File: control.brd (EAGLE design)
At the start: 156 x 38 mm, 67 parts, among them IC3 ATTINY85-20S

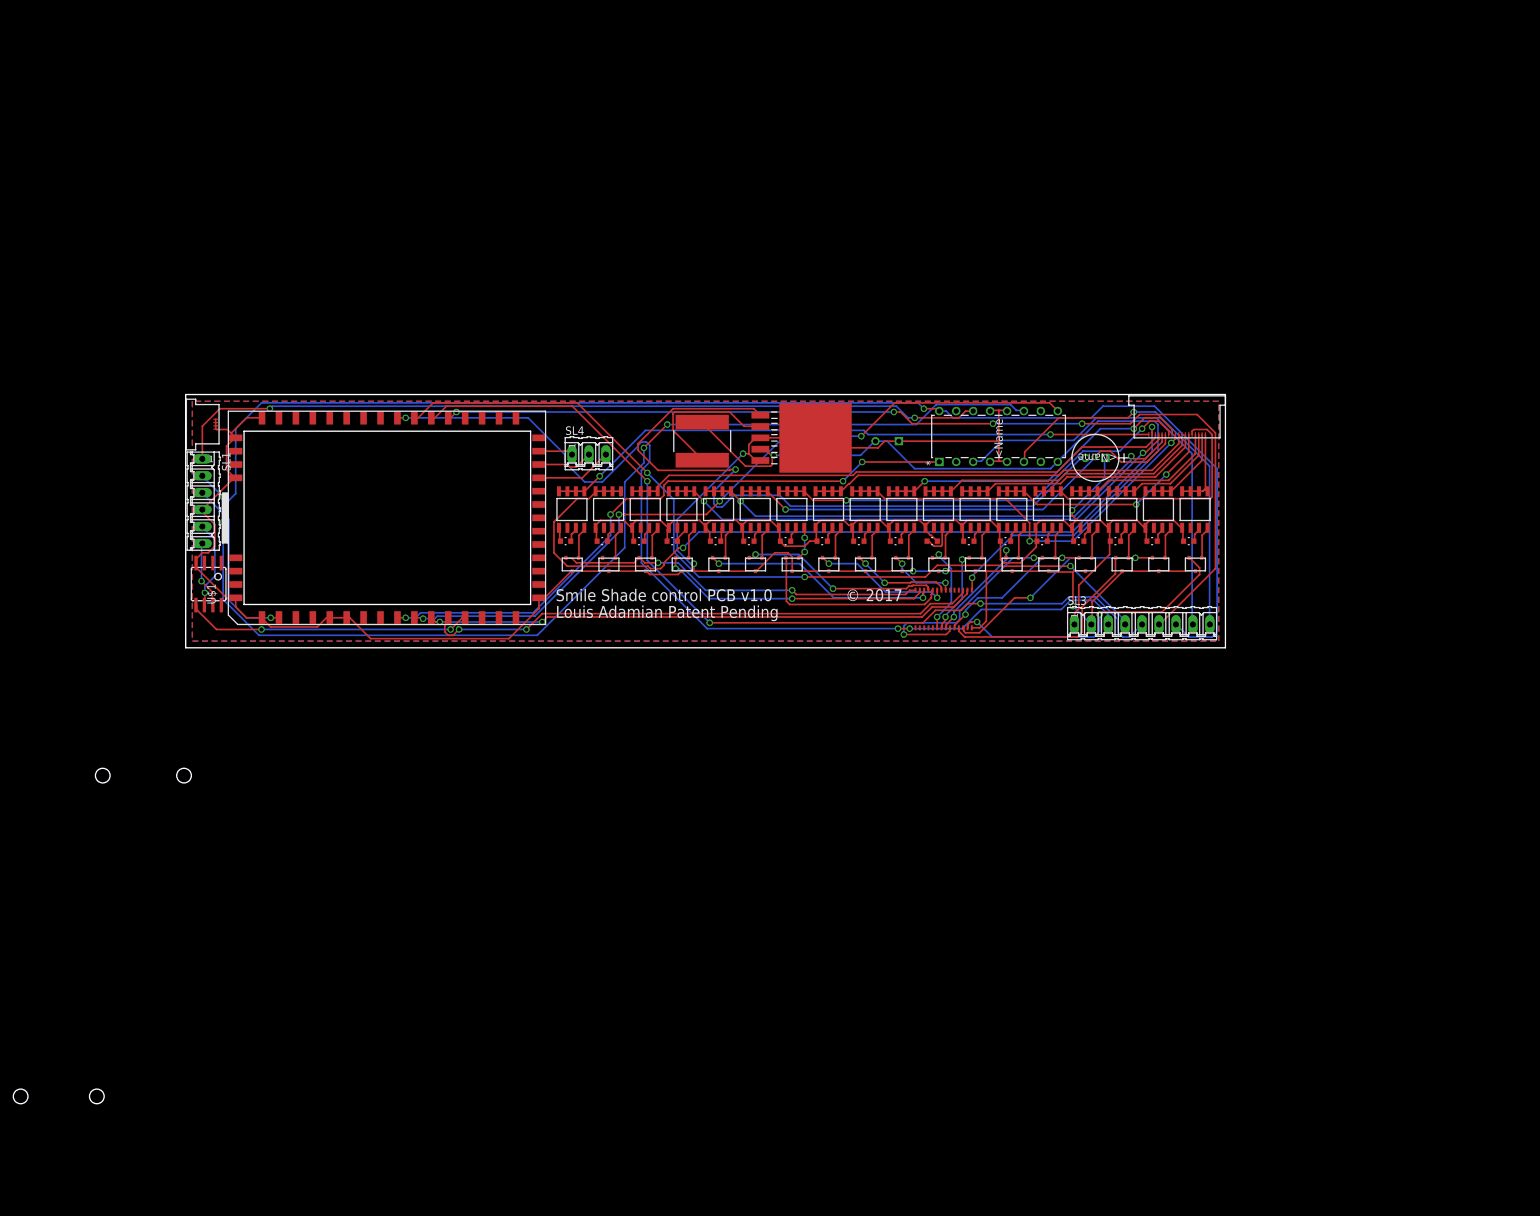
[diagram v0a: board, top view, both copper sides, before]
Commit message: adds new components
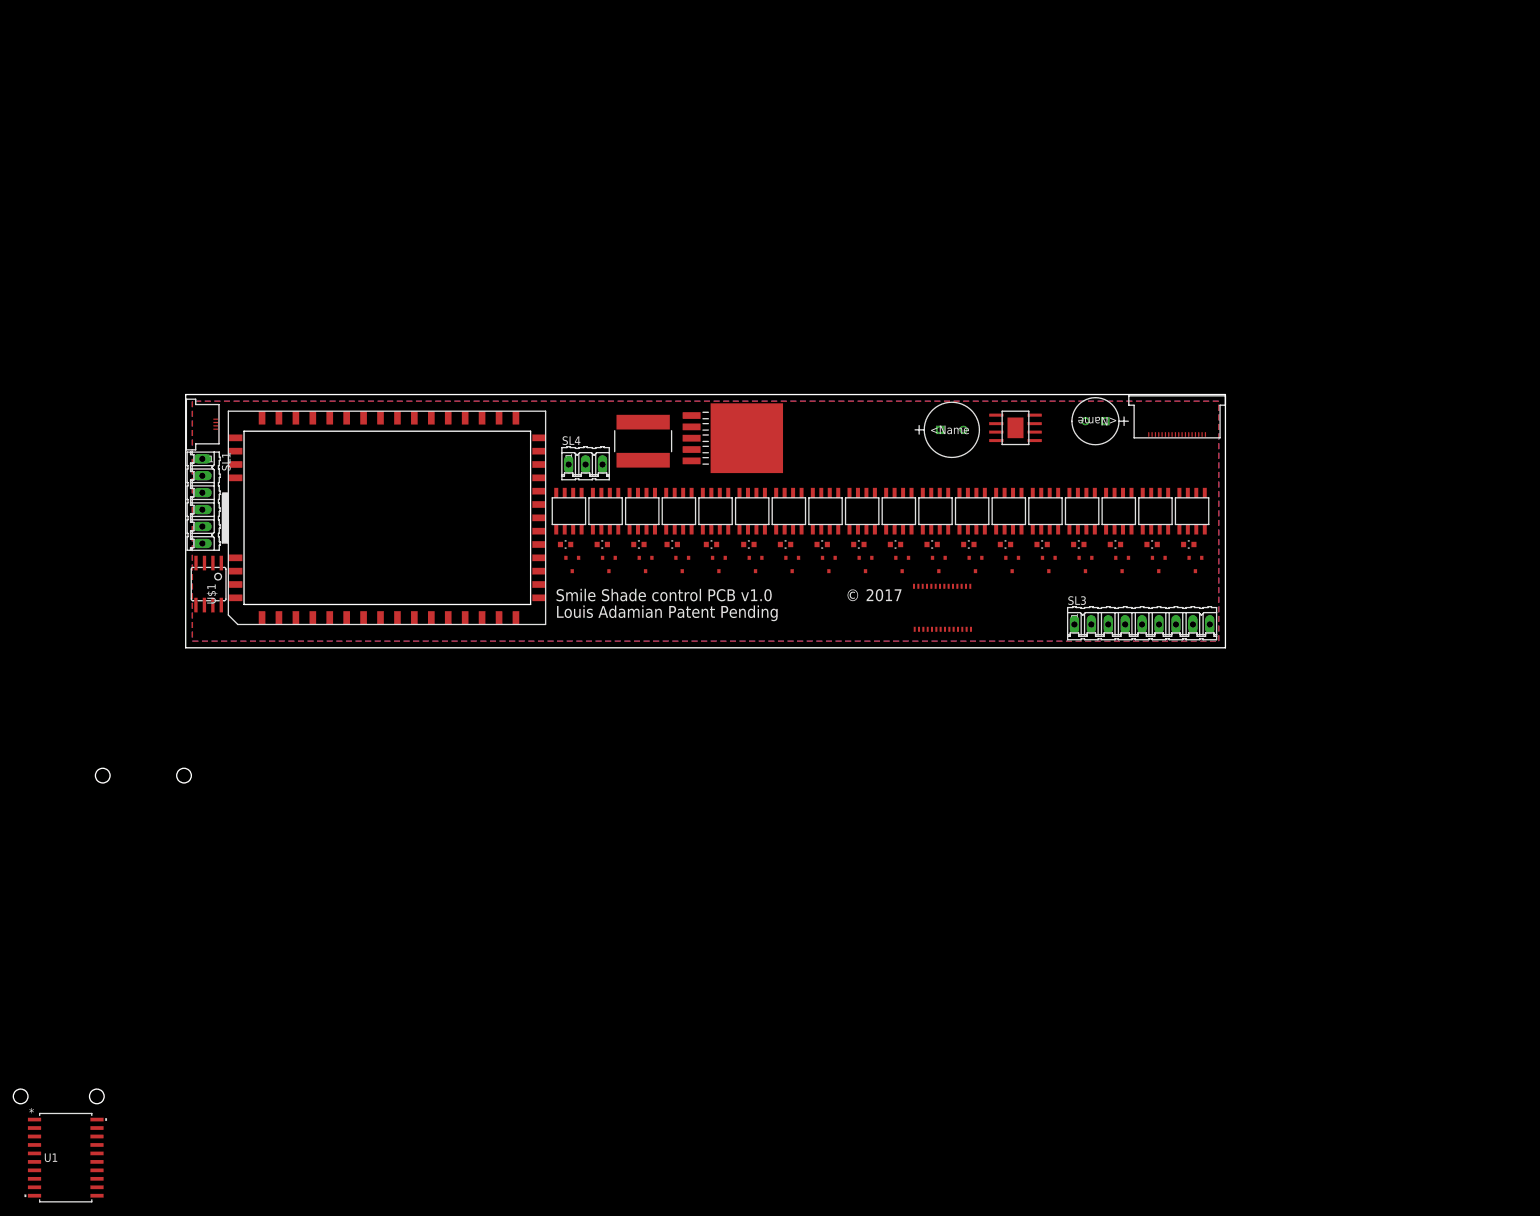
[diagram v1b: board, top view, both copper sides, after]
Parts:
- removed U$2: L293DNE, LED Driver:NE16
- added U$35: NUD4011DR2G, Smile_Shade:8SOIC
- added U1: L293DD013TR, Smile_Shade:SO-20
- U$11, U$13, U$15, U$17, U$19, U$21, U$23, U$25, U$27, U$29, U$3, U$31, U$33, U$40, U$5, U$7, U$9: device LED Driver:8SOIC -> Smile_Shade:8SOIC
- U$42: value NUD4011DR2G -> TPS54560DDAR; device LED Driver:8SOIC -> Smile_Shade:8-S-POWERPAD
- moved U$42 64.8 mm to (124.5, 33.0)
- moved C1 13.3 mm to (116.7, 32.7), flipped to the top
- moved U$43 10.3 mm to (84.2, 31.4)
- moved U$36 8.86 mm to (68.6, 31.0)
- moved U$21 7.43 mm to (107.0, 20.5)
- moved U$25 7.43 mm to (96.0, 20.5)
- moved U$40 7.43 mm to (63.0, 20.5)
- moved C2 5.50 mm to (135.0, 34.0)
- moved U$37 5.00 mm to (113.5, 6.00)
- moved U$19 4.72 mm to (90.5, 20.5)
- moved U$23 4.72 mm to (101.5, 20.5)
- moved U$11 2.92 mm to (123.5, 20.5)
- moved U$13 2.92 mm to (129.0, 20.5)
- moved U$15 2.92 mm to (112.5, 20.5)
- moved U$17 2.92 mm to (151.0, 20.5)
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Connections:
- removed net M0: U$1.PWM0, U$2.1
- new net DIR1B: U1.9
- new net DIR2A: U1.19
- new net DIR2B: U1.12
- new net M2: U$1.PWM1, U1.11
- new net N$42: U1.4, U1.5, U1.6, U1.7
- new net N$43: U1.14, U1.15, U1.16, U1.17
- new net VIN: SL3.1, U$1.CHG-IN, U$42.P$3
- net 3V3: no longer U$2.16
- net 48: now also U$35.P$1; no longer U$40.P$1
- net 48V: now also U$40.P$1; no longer SL3.1, U$42.P$1
- net 5V: now also U1.20; no longer U$2.8
- net DIR1A: now also U1.2; no longer U$2.7
- net GND: now also U$42.P$7; no longer U$2.12, U$2.13, U$2.4, U$2.5
- net LEDSTR_10: now also U$23.P$5, U$23.P$6, U$23.P$7, U$23.P$8; no longer U$21.P$5, U$21.P$6, U$21.P$7, U$21.P$8
- net LEDSTR_11: now also U$21.P$5, U$21.P$6, U$21.P$7, U$21.P$8; no longer U$23.P$5, U$23.P$6, U$23.P$7, U$23.P$8
- net LEDSTR_12: now also U$19.P$5, U$19.P$6, U$19.P$7, U$19.P$8; no longer U$25.P$5, U$25.P$6, U$25.P$7, U$25.P$8
- net LEDSTR_17: now also U$35.P$5, U$35.P$6, U$35.P$7, U$35.P$8; no longer U$40.P$5, U$40.P$6, U$40.P$7, U$40.P$8
- net LEDSTR_18: now also U$40.P$5, U$40.P$6, U$40.P$7, U$40.P$8; no longer U$42.P$5, U$42.P$6, U$42.P$7, U$42.P$8
- net LEDSTR_9: now also U$25.P$5, U$25.P$6, U$25.P$7, U$25.P$8; no longer U$19.P$5, U$19.P$6, U$19.P$7, U$19.P$8
- net M1: now also U$1.PWM0, U1.1; no longer U$1.PWM1, U$2.9
- net M1A: now also U1.3; no longer U$2.3
- net M1B: now also U1.8; no longer U$2.6
- net M2A: now also U1.18; no longer U$2.14
- net M2B: now also U1.13; no longer U$2.11
- net N$17: now also U$25.P$4; no longer U$19.P$4
- net N$18: now also U$25.P$3; no longer U$19.P$3
- net N$19: now also U$23.P$4; no longer U$21.P$4
- net N$20: now also U$23.P$3; no longer U$21.P$3
- net N$21: now also U$21.P$4; no longer U$23.P$4
- net N$22: now also U$21.P$3; no longer U$23.P$3
- net N$23: now also U$19.P$4; no longer U$25.P$4
- net N$24: now also U$19.P$3; no longer U$25.P$3
- net N$35: now also U$35.P$4; no longer U$40.P$4
- net N$36: now also U$35.P$3; no longer U$40.P$3
- net N$37: now also U$40.P$4; no longer U$42.P$4
- net N$38: now also U$40.P$3; no longer U$42.P$3
- net VCC: now also U1.10; no longer U$1.CHG-IN
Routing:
- net GND: track 305.5 -> 0.00 mm, vias 5 -> 0
- net 3V3: track 225.7 -> 0.00 mm, vias 2 -> 0
- net 48V: track 175.2 -> 0.00 mm, vias 1 -> 0
- net M2B: track 164.1 -> 0.00 mm, vias 4 -> 0
- net ENDSTOP3: track 150.2 -> 0.00 mm, vias 4 -> 0
- net ENDSTOP0: track 141.7 -> 0.00 mm, vias 3 -> 0
- net ENDSTOP2: track 133.8 -> 0.00 mm, vias 3 -> 0
- net ENDSTOP1: track 127.8 -> 0.00 mm, vias 3 -> 0
- net M2A: track 122.9 -> 0.00 mm, vias 2 -> 0
- net 5V: track 122.3 -> 0.00 mm, vias 2 -> 0
- net LEDSTR_18: track 119.8 -> 0.00 mm, vias 2 -> 0
- net M1: track 112.1 -> 0.00 mm, vias 4 -> 0
- net N$34: track 104.7 -> 0.00 mm, vias 1 -> 0
- net M0: track 93.7 -> 0.00 mm, vias 4 -> 0
- net LEDSTR_17: track 92.6 -> 0.00 mm, vias 2 -> 0
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
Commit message: adds new LED driver
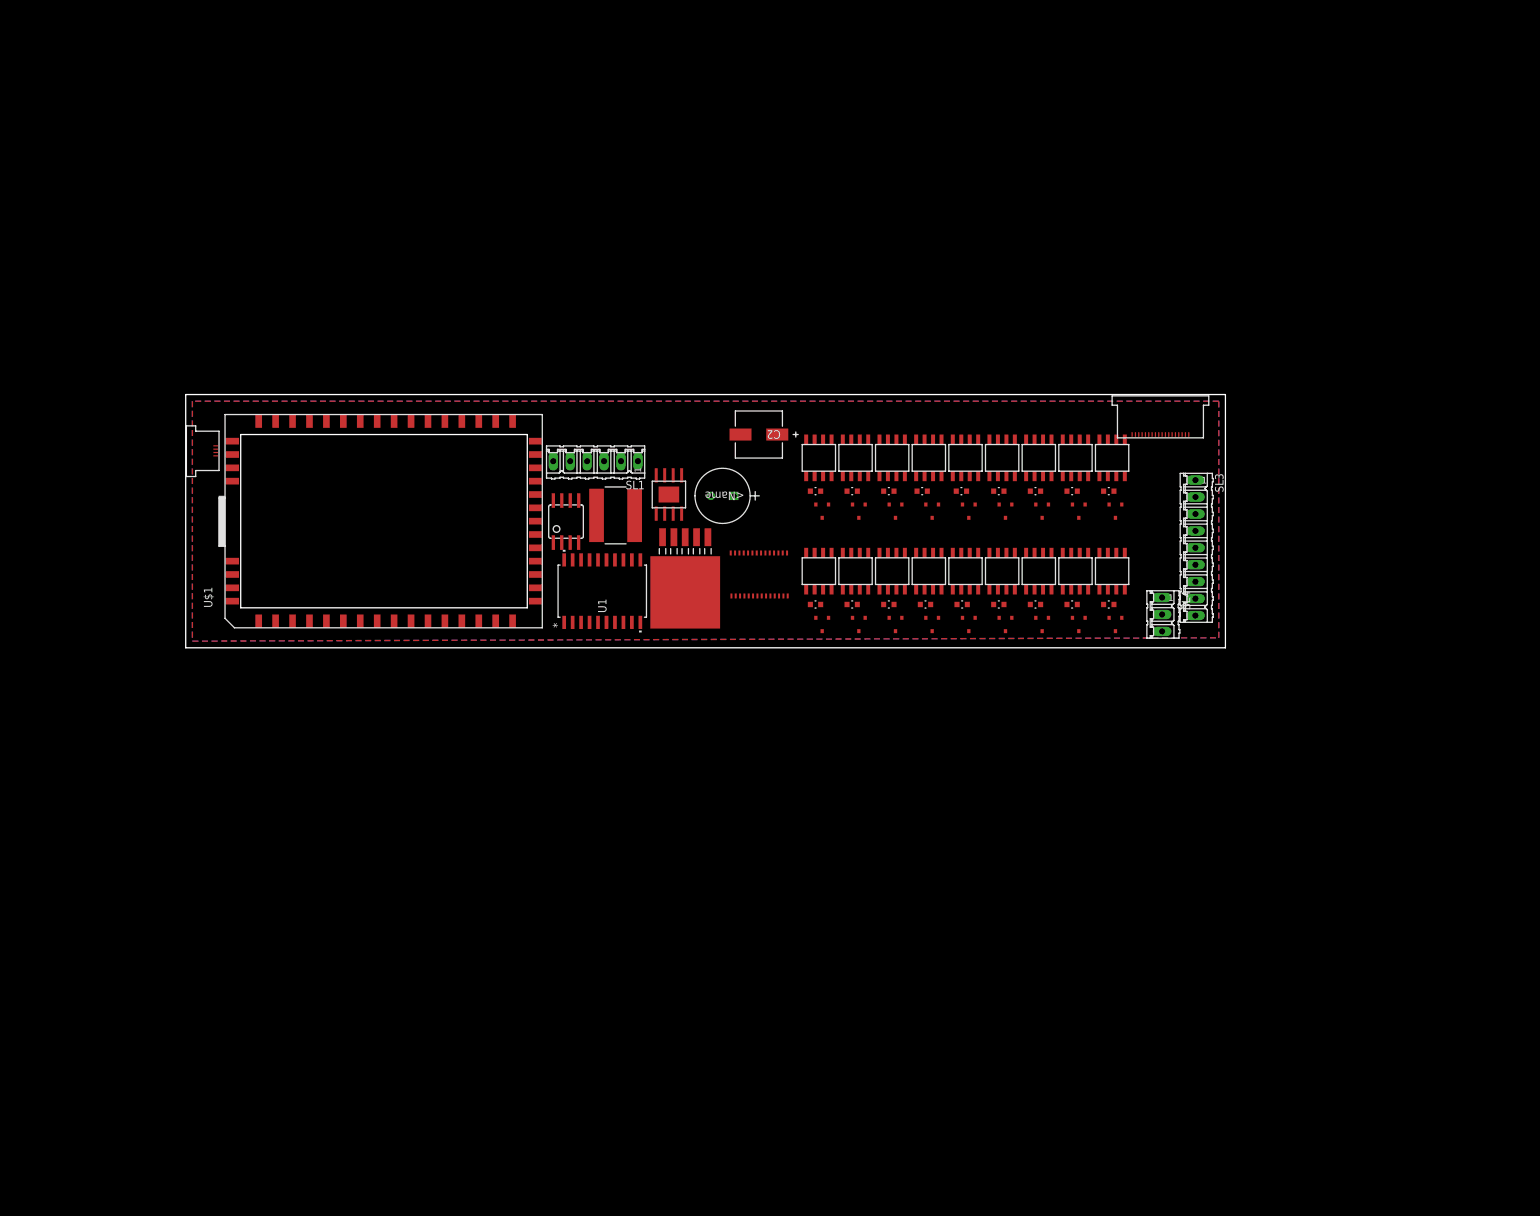
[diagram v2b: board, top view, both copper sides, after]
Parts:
- C2: value ESK107M025AE3EA -> UWX1C101MCL1GB; device Smile_Shade:E-E3 -> Smile_Shade:PCAP_6.3X5.4-ELECT
- moved U1 117.1 mm to (62.5, 8.50), turned to 90 degrees
- moved SL4 89.4 mm to (146.5, 5.00), turned to 270 degrees
- moved SL1 59.3 mm to (61.5, 28.0), turned to 180 degrees
- moved IC3 54.4 mm to (57.1, 18.9), turned to 0 degrees
- moved U$42 53.0 mm to (72.5, 23.0), turned to 90 degrees
- moved C2 49.0 mm to (86.0, 32.0)
- moved C1 39.2 mm to (78.8, 22.8), turned to 180 degrees
- moved R11 38.3 mm to (127.5, 23.5)
- moved R12 38.3 mm to (105.5, 23.5)
- moved R13 38.3 mm to (110.5, 23.5)
- moved R14 38.3 mm to (116.4, 23.5)
- moved R15 38.3 mm to (122.0, 23.5)
- moved R16 38.3 mm to (94.5, 23.5)
- moved R17 38.3 mm to (100.0, 23.5)
- moved R7 38.3 mm to (133.0, 23.5)
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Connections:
- removed net N$42: U1.4, U1.5, U1.6, U1.7
- removed net N$43: U1.14, U1.15, U1.16, U1.17
- net DIR1A: now also U$1.CSID4
- net DIR1B: now also U$1.CSID5
- net DIR2A: now also U$1.CSID6
- net DIR2B: now also U$1.CSID7
- net GND: now also U1.14, U1.15, U1.16, U1.17, U1.4, U1.5, U1.6, U1.7
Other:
- board text removed: "2017"
- board text removed: "©"
